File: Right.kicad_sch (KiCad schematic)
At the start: 27 parts, among them J1 USB_B_Micro, J2 Conn_01x02, U1 NCP1117-3.3_SOT223, U2 W25Q128JVS, U3 RP2040, Y1 ABLS-12.000MHZ-B4-T

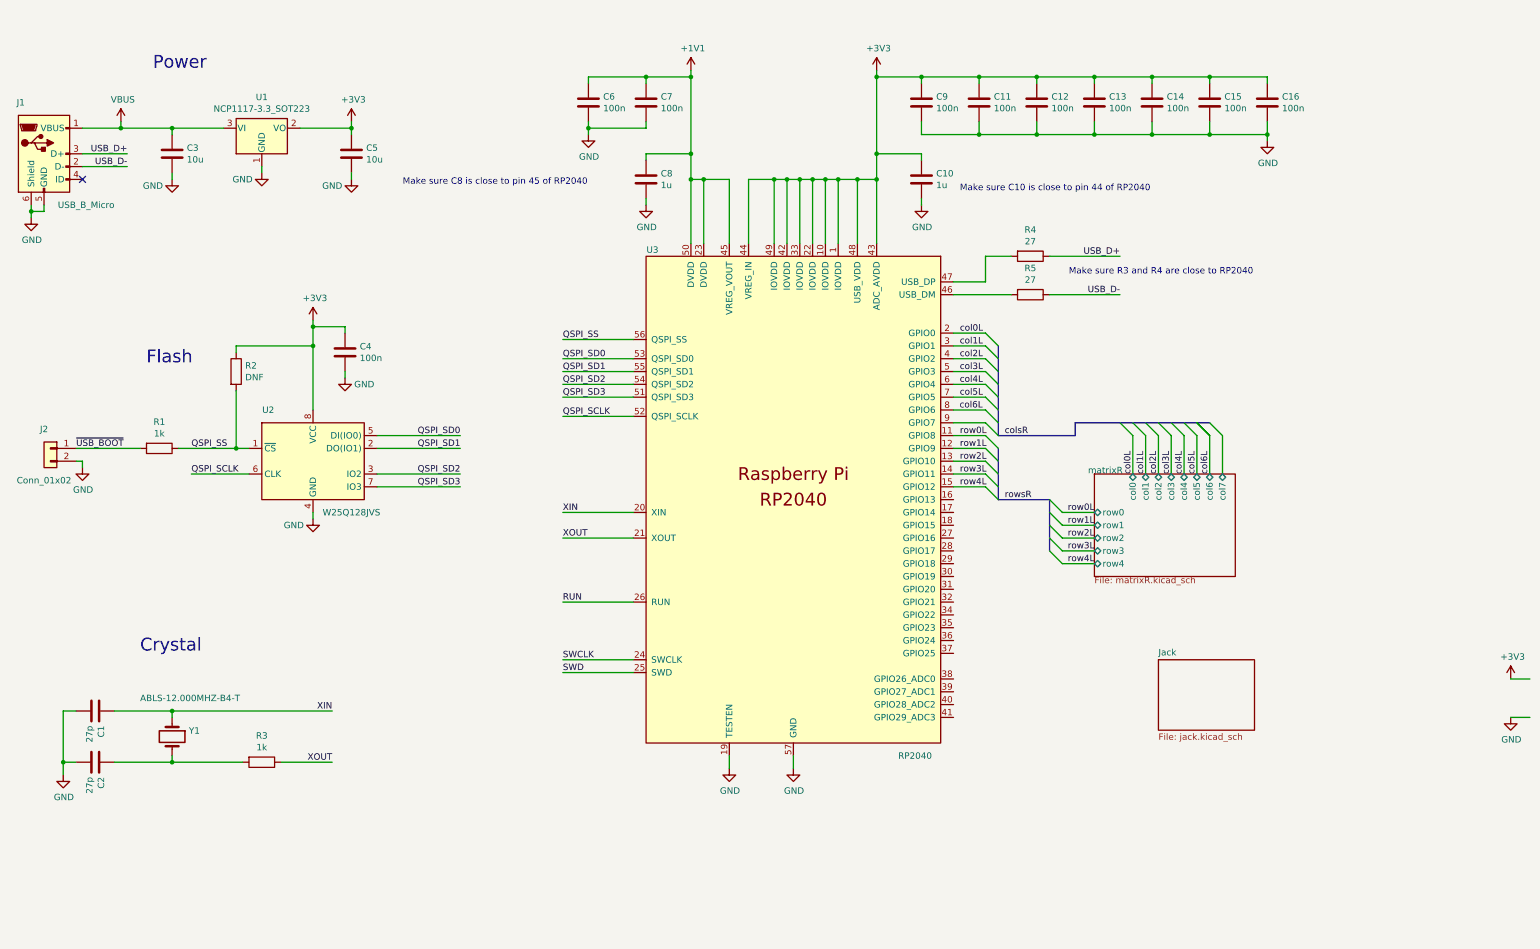
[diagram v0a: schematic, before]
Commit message: Hot pluggable trrs
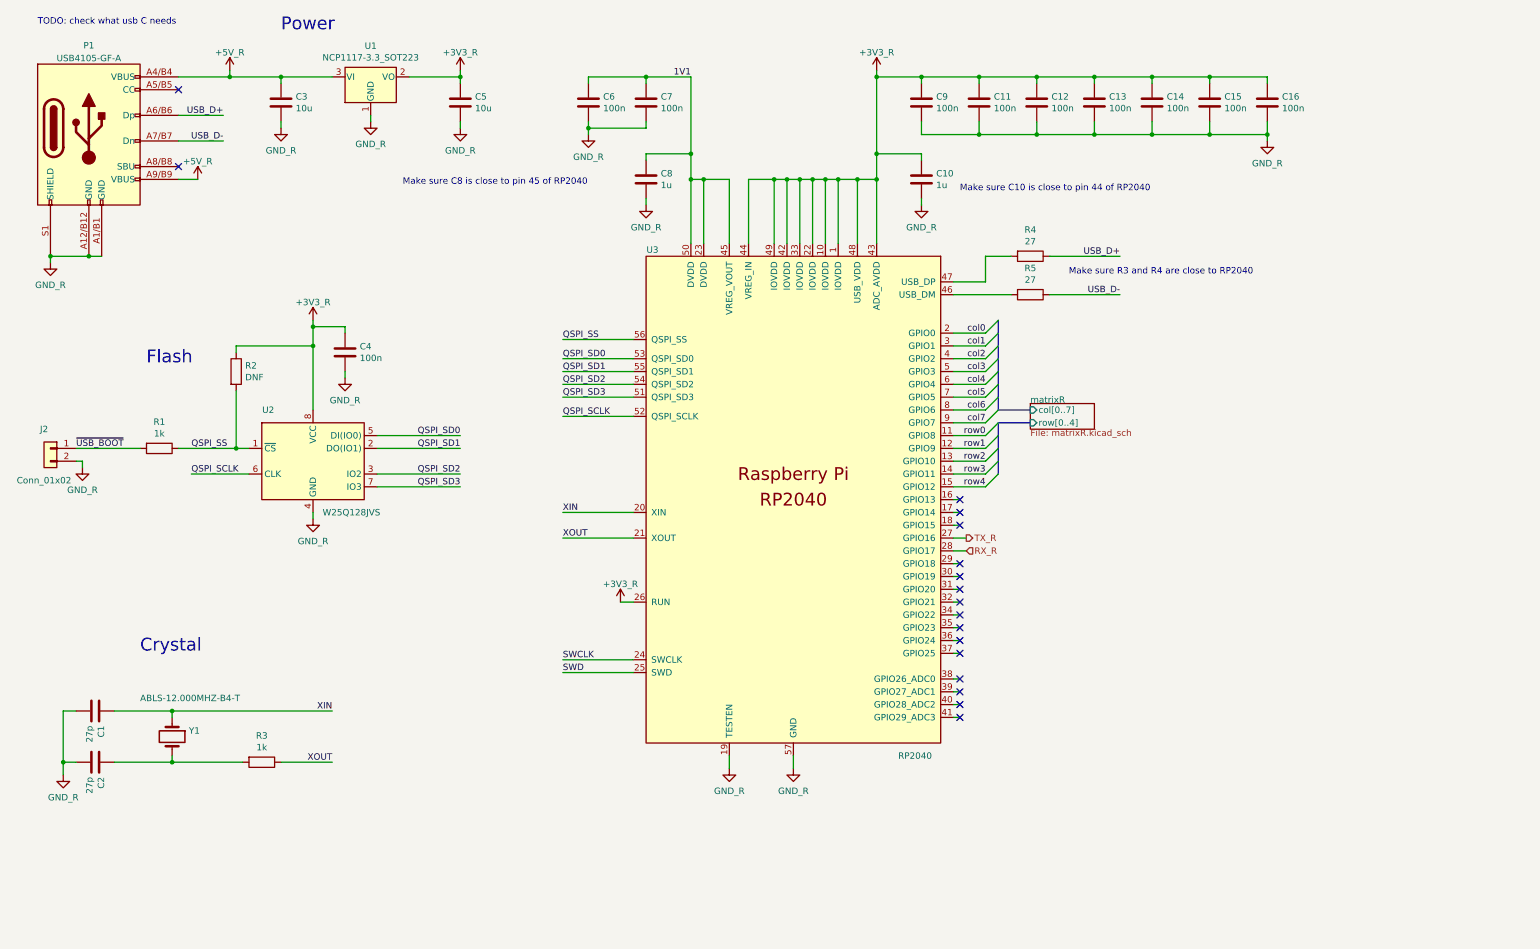
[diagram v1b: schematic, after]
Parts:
- removed J1: USB_B_Micro, RP2040_minimal:USB_Micro-B_Amphenol_10103594-0001LF_Horizontal_modified, symbol RP2040_minimal-rescue:USB_B_Micro-Connector
- added P1: USB4105-GF-A, symbol arisu-split:USB4105-GF-A
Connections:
- net RUN is gone; now on net +3V3_R: U3.26 (RUN)
- net USB_D+: now also P1.A6/B6 (Dp)
- net USB_D-: now also P1.A7/B7 (Dn)
- net TX_R: now reaches U3.27 (GPIO16)
- net RX_R: now reaches U3.28 (GPIO17)
- net col7: now reaches U3.9 (GPIO7)
- net +1V1 renamed 1V1
- net +3V3 renamed +3V3_R
- net GND renamed GND_R
- net GND_R: now also P1.A1/B1 (GND), P1.A12/B12 (GND), P1.S1 (SHIELD)
- net VBUS renamed +5R
- net +5R: now also P1.A4/B4 (VBUS), P1.A9/B9 (VBUS)
- net col0L renamed col0
- net col1L renamed col1
- net col2L renamed col2
- net col3L renamed col3
- net col4L renamed col4
- net col5L renamed col5
- net col6L renamed col6
- net row0L renamed row0
- net row1L renamed row1
- net row2L renamed row2
- net row3L renamed row3
- net row4L renamed row4
- no-connect marks 1 -> 17
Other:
- removed sheet Jack
- sheet matrixR ports: added col[0..7], row[0..4]; removed col0, col1, col2, col3, col4, col5, col6, col7, row0, row1, row2, row3, row4
- note added: "TODO: check what usb C needs"
- moved on the sheet: C3, C5, U1

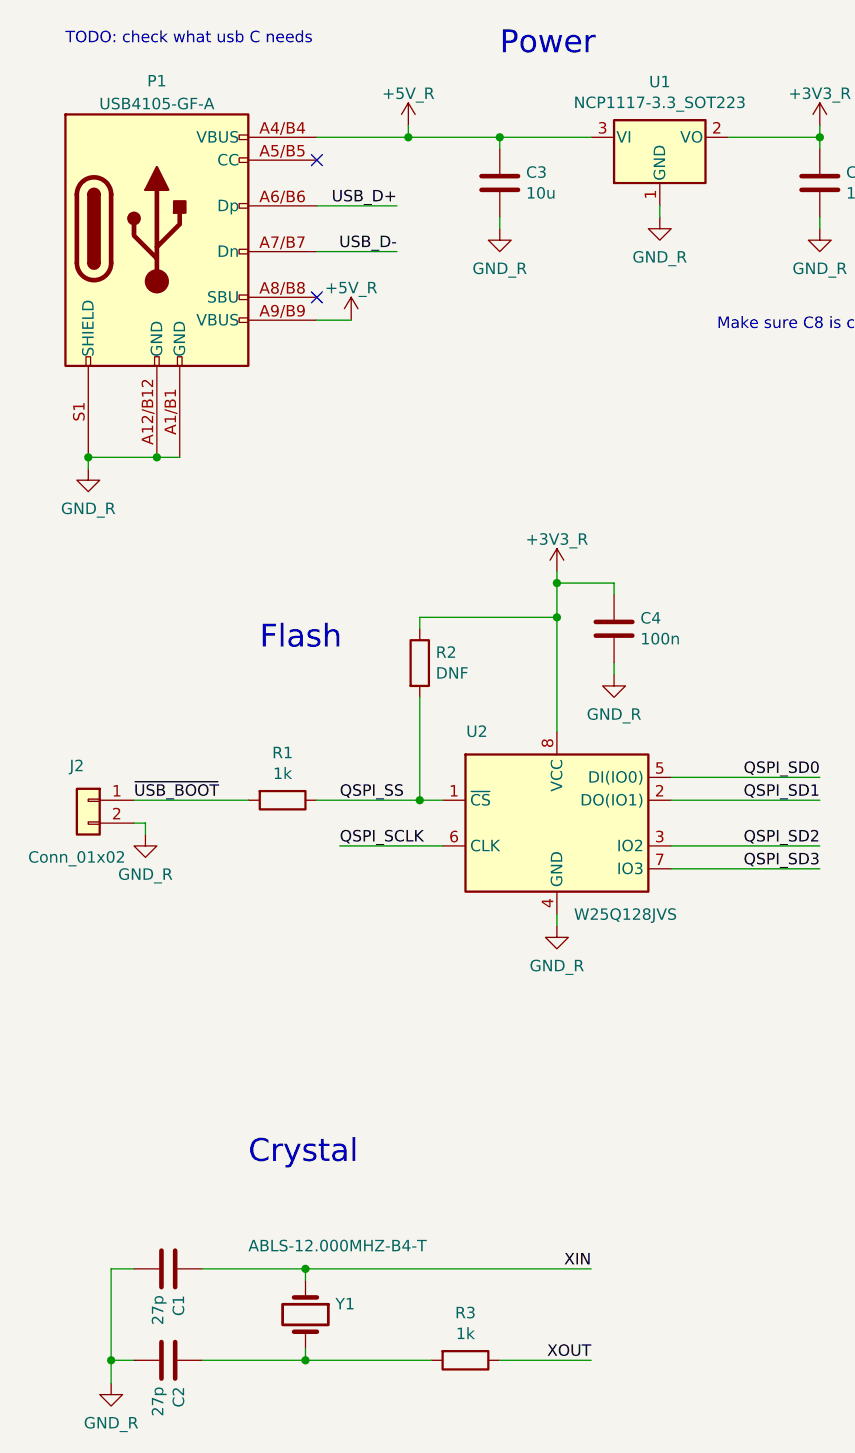
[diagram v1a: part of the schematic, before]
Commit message: Add second micro back in, and added some footprints
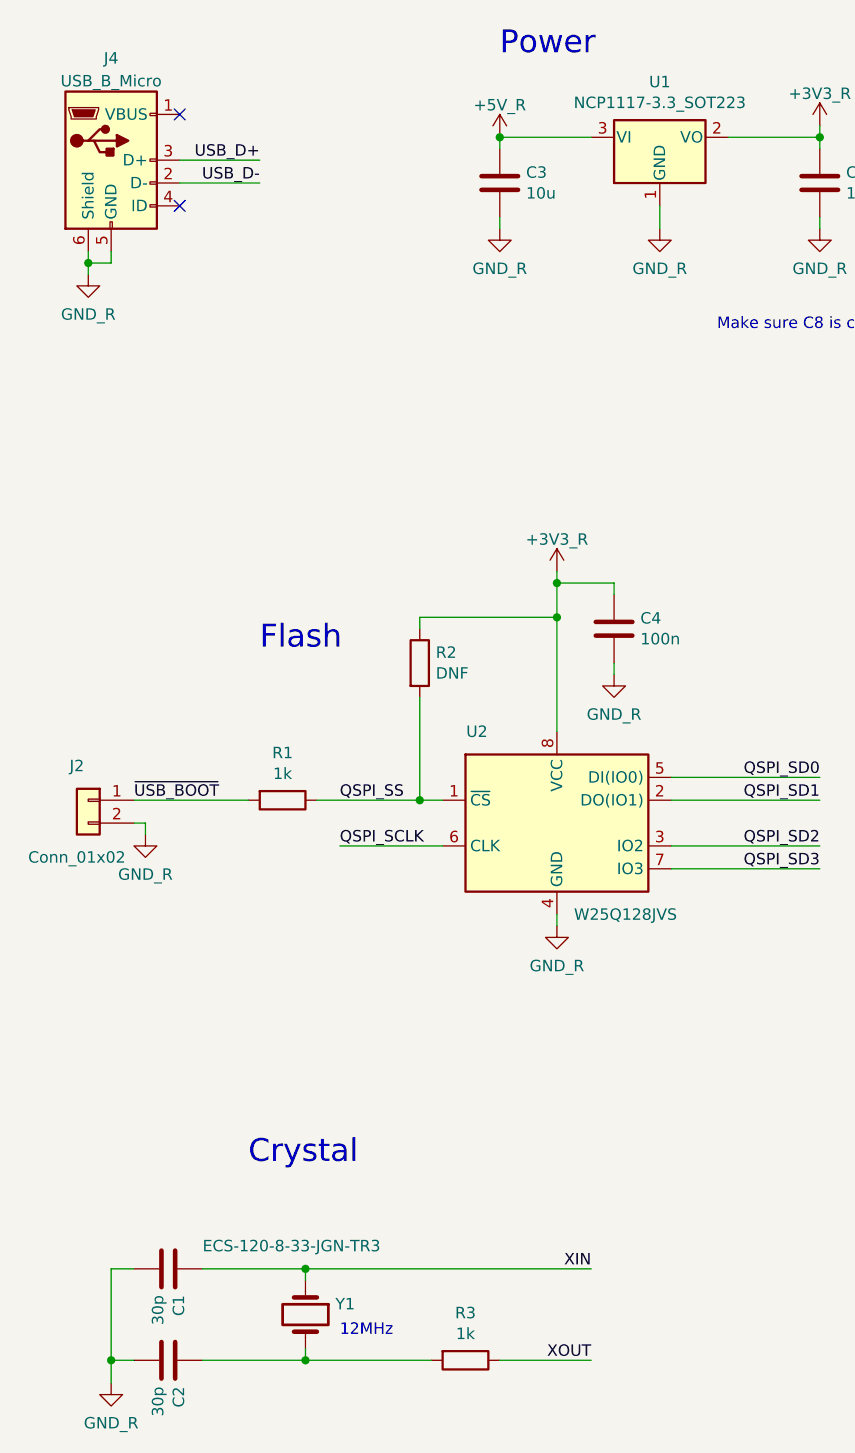
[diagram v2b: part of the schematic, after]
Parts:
- removed P1: USB4105-GF-A, symbol arisu-split:USB4105-GF-A
- added J4: USB_B_Micro, symbol arisu-split:USB_B_Micro
- C1, C2: value 27p -> 30p
- Y1: value ABLS-12.000MHZ-B4-T -> ECS-120-8-33-JGN-TR3; footprint RP2040_minimal:Crystal_SMD_HC49-US -> Crystal:Crystal_SMD_EuroQuartz_MT-4Pin_3.2x2.5mm
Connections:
- net GND_R: now also J4.5 (GND), J4.6 (Shield)
- net USB_D+: now also J4.3 (D+)
- net USB_D-: now also J4.2 (D-)
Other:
- note added: "12MHz"
- note removed: "TODO: check what usb C needs"
